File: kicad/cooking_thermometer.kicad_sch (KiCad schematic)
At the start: 37 parts, among them J1 FTDI, J2 STLINK, J3 3V3_Power, J4 Battery, J5 7SEG_CONN, J6 OLED_CONN, J7 USB_B_Micro, J8 THERMO_CONN, SW1 BOOT0_SW, SW2 NRST_SW, SW3 UI_A_SW, SW4 UI_B_SW, SW5 UI_C_SW, U1 STM32F070F6Px, U2 MCP1700x-330xxTO, U3 MCP73831-2-OT

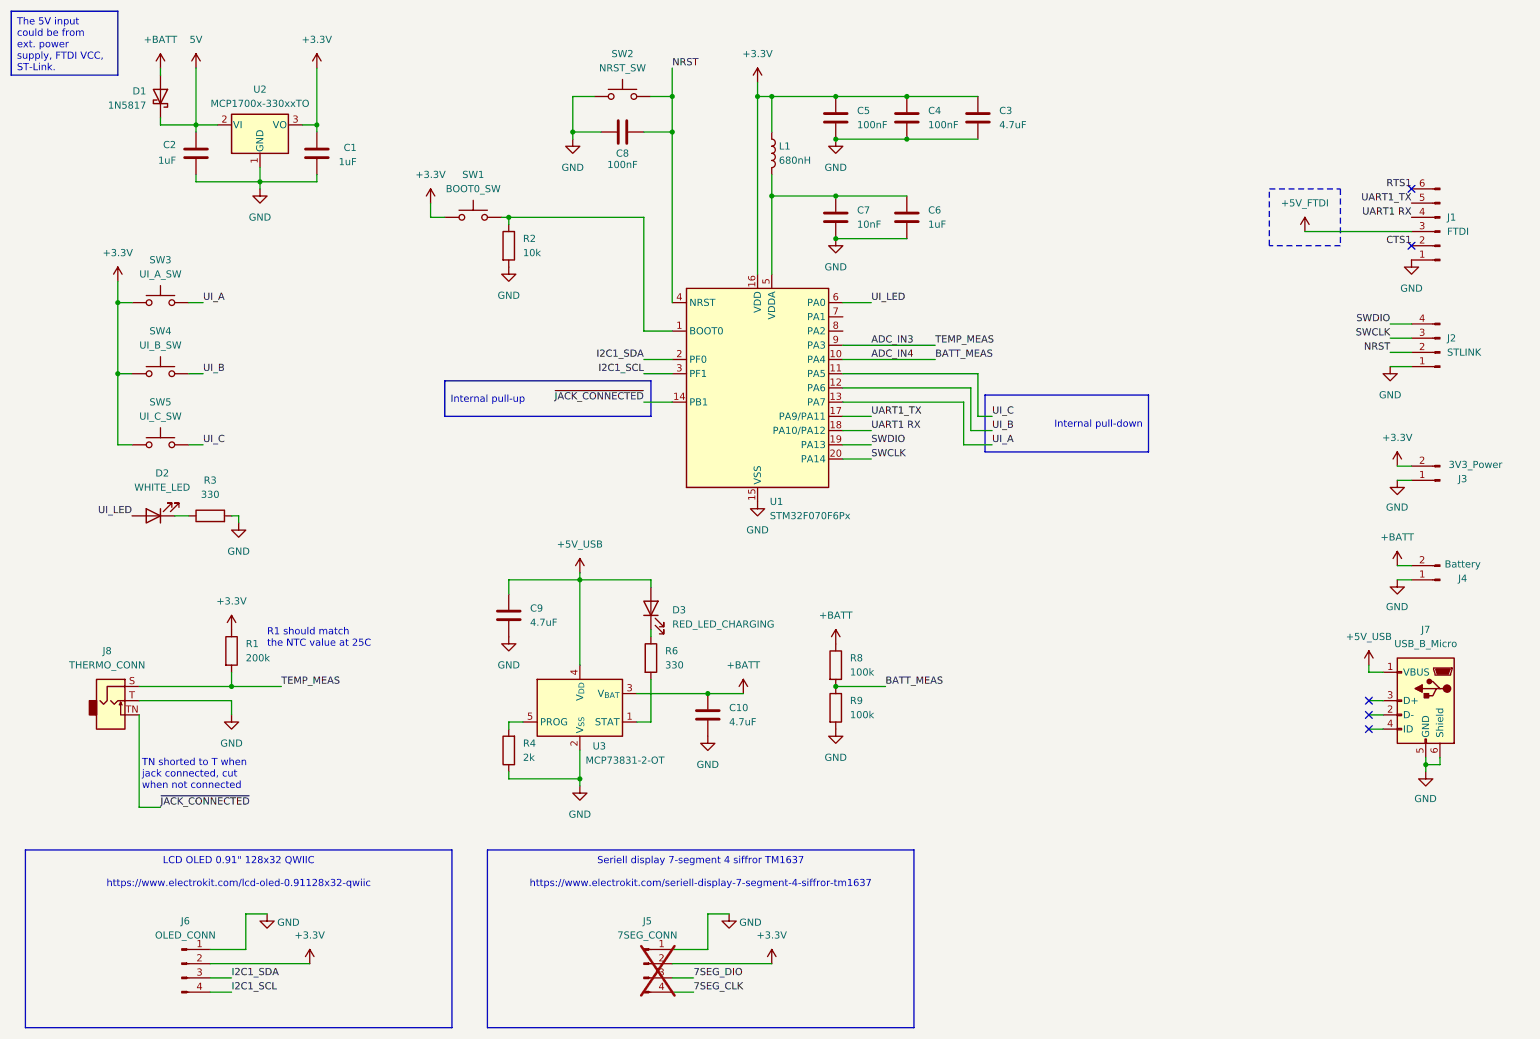
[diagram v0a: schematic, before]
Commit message: Add passive buzzer to schematic, layout, stm32cube
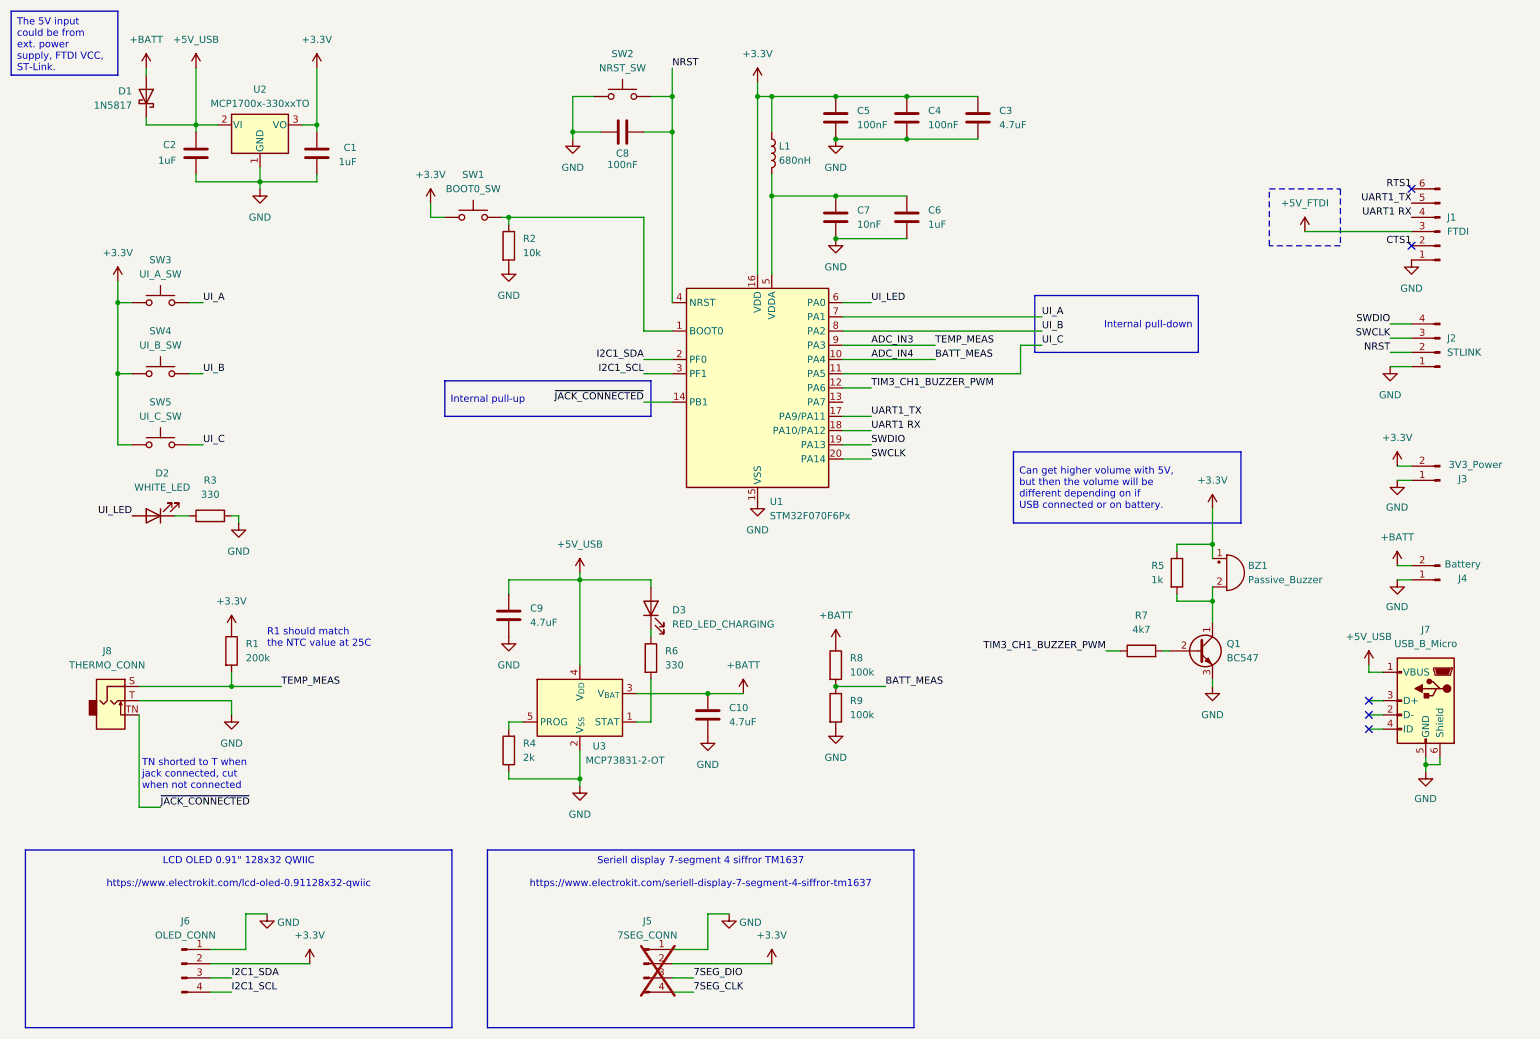
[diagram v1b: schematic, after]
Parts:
- added BZ1: Passive_Buzzer, Buzzer_Beeper:Buzzer_12x9.5RM7.6, symbol Device:Buzzer
- added Q1: BC547, Package_TO_SOT_THT:TO-92L_Inline_Wide, symbol Transistor_BJT:BC547
- added R5: 1k, Resistor_THT:R_Axial_DIN0207_L6.3mm_D2.5mm_P7.62mm_Horizontal, symbol Device:R
- added R7: 4k7, Resistor_THT:R_Axial_DIN0207_L6.3mm_D2.5mm_P7.62mm_Horizontal, symbol Device:R
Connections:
- net 5V is gone; now on net +5V_USB: C2.1, D1.1 (K), U2.2 (VI)
- net +3.3V: now also BZ1.1 (+), R5.1
- net GND: now also Q1.3 (E)
- net UI_A: now also U1.7 (PA1); no longer U1.13 (PA7)
- net UI_B: now also U1.8 (PA2); no longer U1.12 (PA6)
- new net: BZ1.2 (-), Q1.1 (C), R5.2
- new net: Q1.2 (B), R7.2
- new net TIM3_CH1_BUZZER_PWM: R7.1, U1.12 (PA6)
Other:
- moved on the sheet: D1

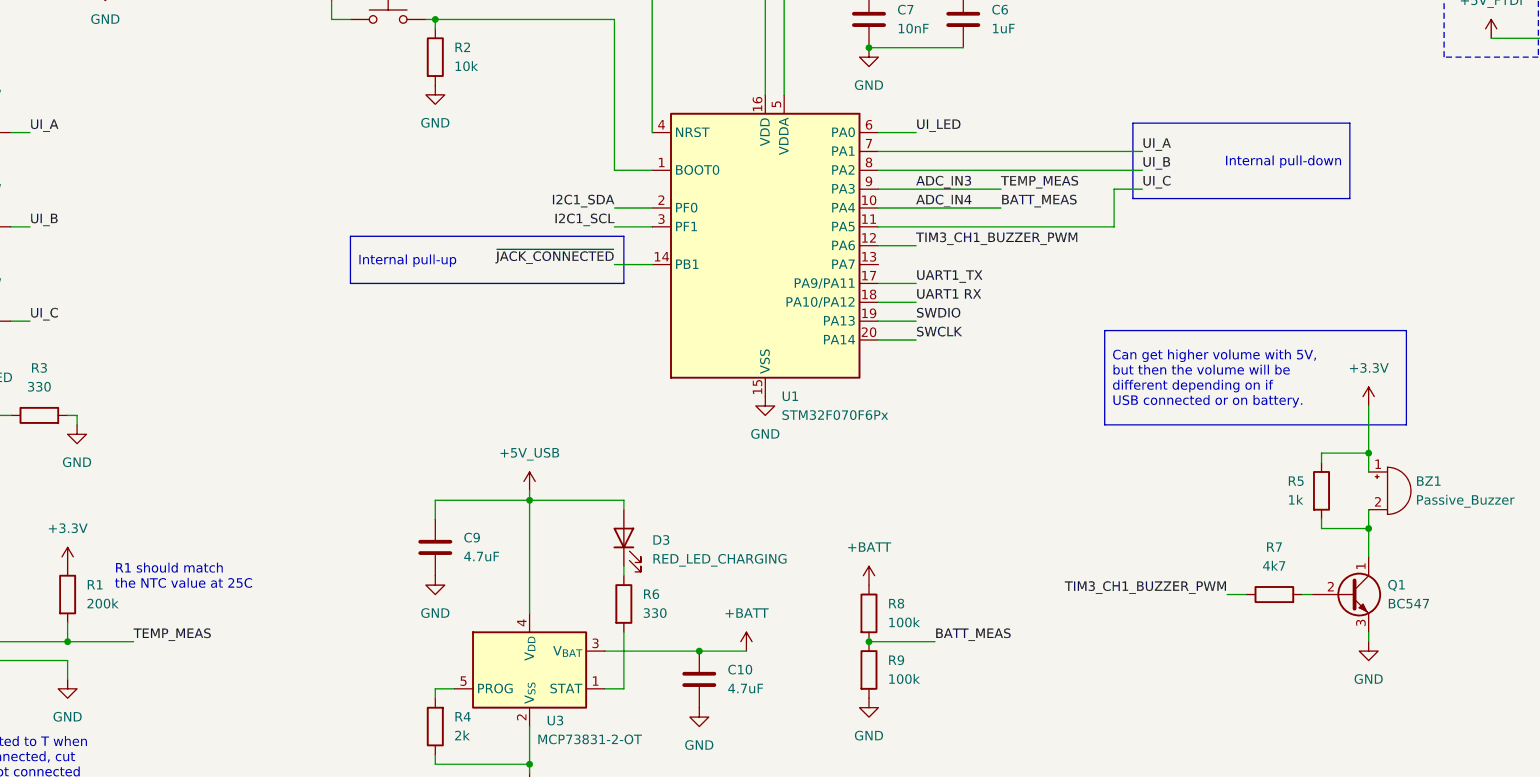
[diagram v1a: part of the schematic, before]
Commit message: Rearrange signals to better fit board
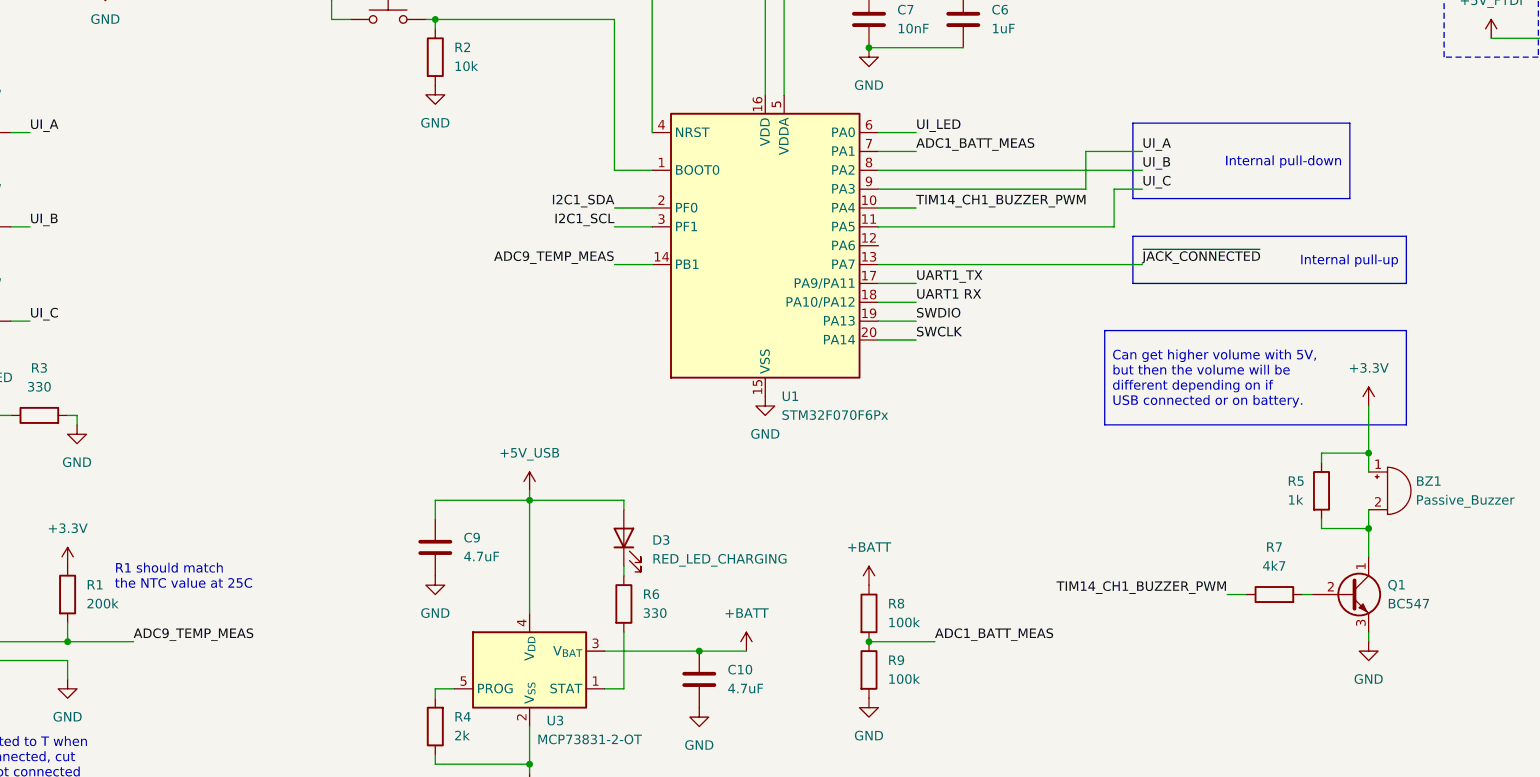
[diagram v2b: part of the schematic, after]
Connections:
- net UI_A: now also U1.9 (PA3); no longer U1.7 (PA1)
- net ~{JACK_CONNECTED}: now also U1.13 (PA7); no longer U1.14 (PB1)
- net ADC_IN3 renamed ADC9_TEMP_MEAS
- net ADC9_TEMP_MEAS: now also U1.14 (PB1); no longer U1.9 (PA3)
- net ADC_IN4 renamed ADC1_BATT_MEAS
- net ADC1_BATT_MEAS: now also U1.7 (PA1); no longer U1.10 (PA4)
- net TIM3_CH1_BUZZER_PWM: no longer names the net of U1.12 (PA6)
- net TIM3_CH1_BUZZER_PWM: no longer R7.1
- new net TIM14_CH1_BUZZER_PWM: R7.1, U1.10 (PA4)
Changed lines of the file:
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@@
+	(wire
+		(pts
+			(xy 190.5 73.66) (xy 162.56 73.66)
+		)
+		(stroke
+			(width 0)
+			(type default)
+		)
+	)
 	(wire
 		(pts
@@
 	(wire
 		(pts
+			(xy 167.64 68.58) (xy 162.56 68.58)
+		)
+		(stroke
+			(width 0)
+			(type default)
+		)
+	)
+	(wire
+		(pts
 			(xy 54.61 105.41) (xy 54.61 104.14)
 		)
@@
 	(wire
 		(pts
+			(xy 127 83.82) (xy 132.08 83.82)
+		)
+		(stroke
+			(width 0)
+			(type default)
+		)
+	)
+	(wire
+		(pts
 			(xy 138.43 175.26) (xy 138.43 181.61)
 		)
@@
 	(wire
 		(pts
-			(xy 162.56 73.66) (xy 179.07 73.66)
-		)
-		(stroke
-			(width 0)
-			(type default)
-		)
-	)
-	(wire
-		(pts
 			(xy 127 71.12) (xy 127 50.8)
 		)
@@
 	(wire
 		(pts
-			(xy 162.56 76.2) (xy 179.07 76.2)
+			(xy 162.56 76.2) (xy 167.64 76.2)
 		)
 		(stroke
@@
 	(wire
 		(pts
+			(xy 162.56 83.82) (xy 198.12 83.82)
+		)
+		(stroke
+			(width 0)
+			(type default)
+		)
+	)
+	(wire
+		(pts
 			(xy 115.57 115.57) (xy 128.27 115.57)
 		)
@@
 	(wire
 		(pts
-			(xy 167.64 81.28) (xy 162.56 81.28)
-		)
-		(stroke
-			(width 0)
-			(type default)
-		)
-	)
-	(wire
-		(pts
 			(xy 260.35 77.47) (xy 264.16 77.47)
 		)
@@
 	(wire
 		(pts
-			(xy 127 83.82) (xy 132.08 83.82)
+			(xy 198.12 68.58) (xy 190.5 68.58)
 		)
 		(stroke
@@
 	(wire
 		(pts
-			(xy 198.12 68.58) (xy 162.56 68.58)
-		)
-		(stroke
-			(width 0)
-			(type default)
-		)
-	)
-	(wire
-		(pts
 			(xy 114.3 35.56) (xy 119.38 35.56)
 		)
@@
 		(pts
 			(xy 222.25 119.38) (xy 222.25 118.11)
+		)
+		(stroke
+			(width 0)
+			(type default)
+		)
+	)
+	(wire
+		(pts
+			(xy 190.5 68.58) (xy 190.5 73.66)
 		)
 		(stroke
@@
 	(text_box "Internal pull-up"
 		(exclude_from_sim no)
-		(at 91.44 80.01 0)
+		(at 196.85 80.01 0)
 		(size 36.83 6.35)
 		(stroke
@@
 				(size 1.27 1.27)
 			)
-			(justify left)
+			(justify right)
 		)
 	)
@@
 		)
 	)
+	(label "ADC9_TEMP_MEAS"
+		(at 127 83.82 180)
+		(fields_autoplaced yes)
+		(effects
+			(font
+				(size 1.27 1.27)
+			)
+			(justify right bottom)
+		)
+	)
 	(label "NRST"
 		(at 132.08 24.13 0)
@@
 		)
 	)
-	(label "BATT_MEAS"
-		(at 179.07 76.2 0)
+	(label "TIM14_CH1_BUZZER_PWM"
+		(at 167.64 76.2 0)
 		(fields_autoplaced yes)
 		(effects
@@
 		)
 	)
-	(label "TIM3_CH1_BUZZER_PWM"
-		(at 167.64 81.28 0)
-		(fields_autoplaced yes)
-		(effects
-			(font
-				(size 1.27 1.27)
-			)
-			(justify left bottom)
-		)
-	)
 	(label "I2C1_SDA"
 		(at 127 76.2 180)
@@
 		)
 	)
-	(label "TIM3_CH1_BUZZER_PWM"
+	(label "TIM14_CH1_BUZZER_PWM"
 		(at 209.55 128.27 180)
 		(fields_autoplaced yes)
@@
 			)
 			(justify right bottom)
-		)
-	)
-	(label "ADC_IN3"
-		(at 167.64 73.66 0)
-		(fields_autoplaced yes)
-		(effects
-			(font
-				(size 1.27 1.27)
-			)
-			(justify left bottom)
 		)
 	)
@@
 		)
 	)
-	(label "TEMP_MEAS"
+	(label "ADC9_TEMP_MEAS"
 		(at 62.23 134.62 0)
 		(fields_autoplaced yes)
@@
 		)
 	)
+	(label "ADC1_BATT_MEAS"
+		(at 167.64 68.58 0)
+		(fields_autoplaced yes)
+		(effects
+			(font
+				(size 1.27 1.27)
+			)
+			(justify left bottom)
+		)
+	)
+	(label "~{JACK_CONNECTED}"
+		(at 198.12 83.82 0)
+		(fields_autoplaced yes)
+		(effects
+			(font
+				(size 1.27 1.27)
+			)
+			(justify left bottom)
+		)
+	)
 	(label "CTS1"
 		(at 264.16 55.88 180)
@@
 		)
 	)
-	(label "ADC_IN4"
-		(at 167.64 76.2 0)
-		(fields_autoplaced yes)
-		(effects
-			(font
-				(size 1.27 1.27)
-			)
-			(justify left bottom)
-		)
-	)
 	(label "UI_C"
 		(at 48.26 91.44 0)
@@
 		)
 	)
-	(label "BATT_MEAS"
+	(label "ADC1_BATT_MEAS"
 		(at 170.18 134.62 0)
 		(fields_autoplaced yes)
@@
 		)
 	)
-	(label "~{JACK_CONNECTED}"
-		(at 127 83.82 180)
-		(fields_autoplaced yes)
-		(effects
-			(font
-				(size 1.27 1.27)
-			)
-			(justify right bottom)
-		)
-	)
 	(label "7SEG_DIO"
 		(at 135.89 186.69 0)
@@
 		(fields_autoplaced yes)
 		(effects
-			(font
-				(size 1.27 1.27)
-			)
-			(justify left bottom)
-		)
-	)
-	(label "TEMP_MEAS"
-		(at 179.07 73.66 0)
-		(fields_autoplaced yes)
-		(effects
